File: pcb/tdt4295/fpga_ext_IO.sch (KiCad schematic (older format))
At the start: 44 parts, among them J501 618015330923, J502 FPGA GPIO, U501 NUP4114UCW1T2G, U502 NUP4114UCW1T2G, U503 NUP4114UCW1T2G, U504 NUP4114UCW1T2G

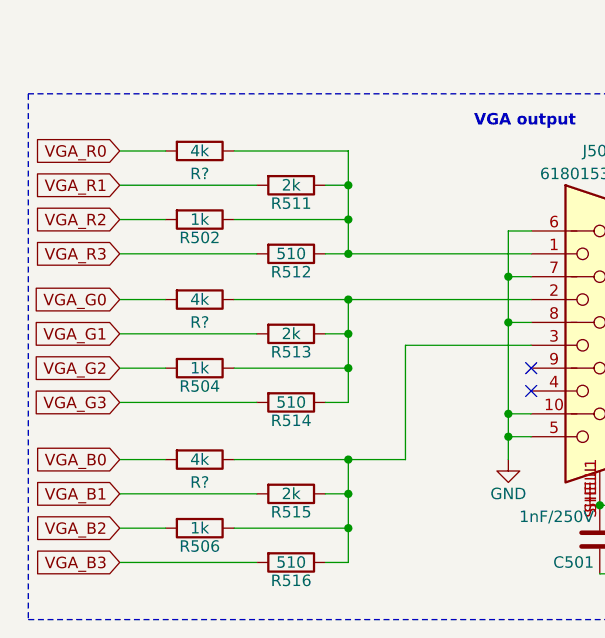
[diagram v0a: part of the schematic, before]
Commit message: placing out components, more routing from FPGA
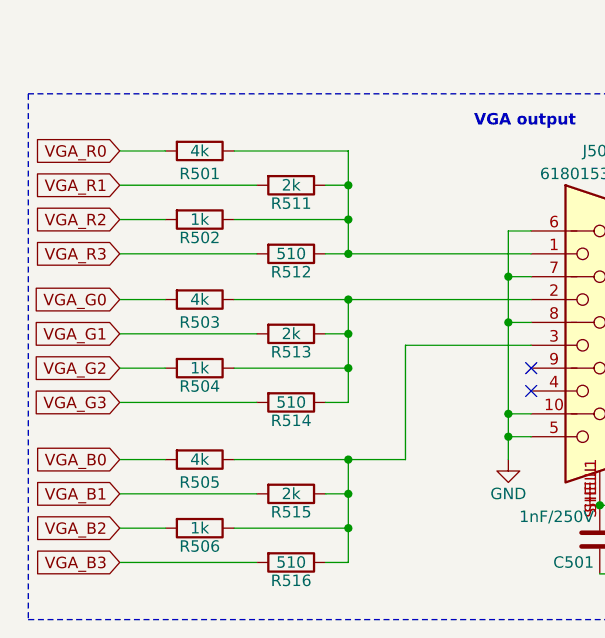
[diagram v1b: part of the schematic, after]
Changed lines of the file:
@@
 $Descr A4 11693 8268
 encoding utf-8
-Sheet 3 6
+Sheet 5 6
 Title ""
 Date ""
@@
 AR Path="/61537853/615B3EE9" Ref="R?"  Part="1"
 AR Path="/617F72AC/61537853/615B3EE9" Ref="R501"  Part="1"
-F 0 "R?" V 1400 4500 50  0000 C CNN
+F 0 "R501" V 1400 4500 50  0000 C CNN
 F 1 "4k" V 1300 4500 50  0000 C CNN
 F 2 "Resistor_SMD:R_1206_3216Metric_Pad1.30x1.75mm_HandSolder" V 1230 4500 50  0001 C CNN
@@
 AR Path="/61537853/615EF461" Ref="R?"  Part="1"
 AR Path="/617F72AC/61537853/615EF461" Ref="R503"  Part="1"
-F 0 "R?" V 1400 5150 50  0000 C CNN
+F 0 "R503" V 1400 5150 50  0000 C CNN
 F 1 "4k" V 1300 5150 50  0000 C CNN
 F 2 "Resistor_SMD:R_1206_3216Metric_Pad1.30x1.75mm_HandSolder" V 1230 5150 50  0001 C CNN
@@
 AR Path="/61537853/615FE017" Ref="R?"  Part="1"
 AR Path="/617F72AC/61537853/615FE017" Ref="R505"  Part="1"
-F 0 "R?" V 1400 5850 50  0000 C CNN
+F 0 "R505" V 1400 5850 50  0000 C CNN
 F 1 "4k" V 1300 5850 50  0000 C CNN
 F 2 "Resistor_SMD:R_1206_3216Metric_Pad1.30x1.75mm_HandSolder" V 1230 5850 50  0001 C CNN

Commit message: assorted minor fixes
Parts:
- U501, U502, U503, U504: symbol tdt4295-rescue:NUP4114UCW1T2G-NUP4114UCW1T2G -> tdt4295-rescue:NUP4114UCW1T2G-NUP4114UCW1T2G-tdt4295-rescue
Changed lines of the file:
@@
 VGA output
 $Comp
-L tdt4295-rescue:NUP4114UCW1T2G-NUP4114UCW1T2G U501
+L tdt4295-rescue:NUP4114UCW1T2G-NUP4114UCW1T2G-tdt4295-rescue U501
 U 1 1 61ADFC51
 P 5650 2900
@@
 $EndComp
 $Comp
-L tdt4295-rescue:NUP4114UCW1T2G-NUP4114UCW1T2G U502
+L tdt4295-rescue:NUP4114UCW1T2G-NUP4114UCW1T2G-tdt4295-rescue U502
 U 1 1 61B06D56
 P 5800 1100
@@
 FPGA_EXT_IO13
 $Comp
-L tdt4295-rescue:NUP4114UCW1T2G-NUP4114UCW1T2G U504
+L tdt4295-rescue:NUP4114UCW1T2G-NUP4114UCW1T2G-tdt4295-rescue U504
 U 1 1 61B47BBA
 P 8000 3200
@@
 	7050 2250 7400 2250
 $Comp
-L tdt4295-rescue:NUP4114UCW1T2G-NUP4114UCW1T2G U503
+L tdt4295-rescue:NUP4114UCW1T2G-NUP4114UCW1T2G-tdt4295-rescue U503
 U 1 1 61BB530D
 P 8000 1100

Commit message: draw most pinouts for FPGA, place capacitors
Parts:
- removed R520, R521, R522, R523, R524, R525, R526, R527, R528, R529, R530, R531, R532, R533: 200, Resistor_SMD:R_2512_6332Metric_Pad1.40x3.35mm_HandSolder, symbol Device:R
- U501, U502, U503, U504: symbol tdt4295-rescue:NUP4114UCW1T2G-NUP4114UCW1T2G-tdt4295-rescue -> tdt4295-rescue:NUP4114UCW1T2G-NUP4114UCW1T2G-tdt4295-rescue-tdt4295-rescue
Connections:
- net FPGA_EXT_IO0: now also J502.1 (Pin_1), U502.1 (I/0_1)
- net FPGA_EXT_IO1: now also J502.3 (Pin_3), U502.6 (I/0_2)
- net FPGA_EXT_IO10: now also J502.8 (Pin_8), U503.3 (I/0_3)
- net FPGA_EXT_IO11: now also J502.10 (Pin_10), U504.1 (I/0_1)
- net FPGA_EXT_IO12: now also J502.12 (Pin_12), U504.6 (I/0_2)
- net FPGA_EXT_IO13: now also J502.14 (Pin_14), U504.3 (I/0_3)
- net FPGA_EXT_IO2: now also J502.5 (Pin_5), U502.4 (I/0_4)
- net FPGA_EXT_IO3: now also J502.7 (Pin_7), U502.3 (I/0_3)
- net FPGA_EXT_IO4: now also J502.9 (Pin_9), U501.1 (I/0_1)
- net FPGA_EXT_IO5: now also J502.11 (Pin_11), U501.6 (I/0_2)
- net FPGA_EXT_IO6: now also J502.13 (Pin_13), U501.3 (I/0_3)
- net FPGA_EXT_IO7: now also J502.2 (Pin_2), U503.1 (I/0_1)
- net FPGA_EXT_IO8: now also J502.4 (Pin_4), U503.6 (I/0_2)
- net FPGA_EXT_IO9: now also J502.6 (Pin_6), U503.4 (I/0_4)

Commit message: put in some 3d models, mostly for fun
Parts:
- U501, U502, U503, U504: symbol tdt4295-rescue:NUP4114UCW1T2G-NUP4114UCW1T2G-tdt4295-rescue-tdt4295-rescue -> tdt4295-rescue:NUP4114UCW1T2G-NUP4114UCW1T2G-tdt4295-rescue-tdt4295-rescue-tdt4295-rescue
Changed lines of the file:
@@
 VGA output
 $Comp
-L tdt4295-rescue:NUP4114UCW1T2G-NUP4114UCW1T2G-tdt4295-rescue-tdt4295-rescue U501
+L tdt4295-rescue:NUP4114UCW1T2G-NUP4114UCW1T2G-tdt4295-rescue-tdt4295-rescue-tdt4295-rescue U501
 U 1 1 61ADFC51
 P 5650 2900
@@
 $EndComp
 $Comp
-L tdt4295-rescue:NUP4114UCW1T2G-NUP4114UCW1T2G-tdt4295-rescue-tdt4295-rescue U502
+L tdt4295-rescue:NUP4114UCW1T2G-NUP4114UCW1T2G-tdt4295-rescue-tdt4295-rescue-tdt4295-rescue U502
 U 1 1 61B06D56
 P 5800 1100
@@
 FPGA_EXT_IO13
 $Comp
-L tdt4295-rescue:NUP4114UCW1T2G-NUP4114UCW1T2G-tdt4295-rescue-tdt4295-rescue U504
+L tdt4295-rescue:NUP4114UCW1T2G-NUP4114UCW1T2G-tdt4295-rescue-tdt4295-rescue-tdt4295-rescue U504
 U 1 1 61B47BBA
 P 8000 3200
@@
 	7050 2250 7400 2250
 $Comp
-L tdt4295-rescue:NUP4114UCW1T2G-NUP4114UCW1T2G-tdt4295-rescue-tdt4295-rescue U503
+L tdt4295-rescue:NUP4114UCW1T2G-NUP4114UCW1T2G-tdt4295-rescue-tdt4295-rescue-tdt4295-rescue U503
 U 1 1 61BB530D
 P 8000 1100
